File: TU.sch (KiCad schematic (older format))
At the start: 5 parts, among them J1 Conn_01x06_Male, J2 Conn_01x06_Male, J3 Conn_Coaxial, J4 Debugger, SW1 SW_DPST_x2

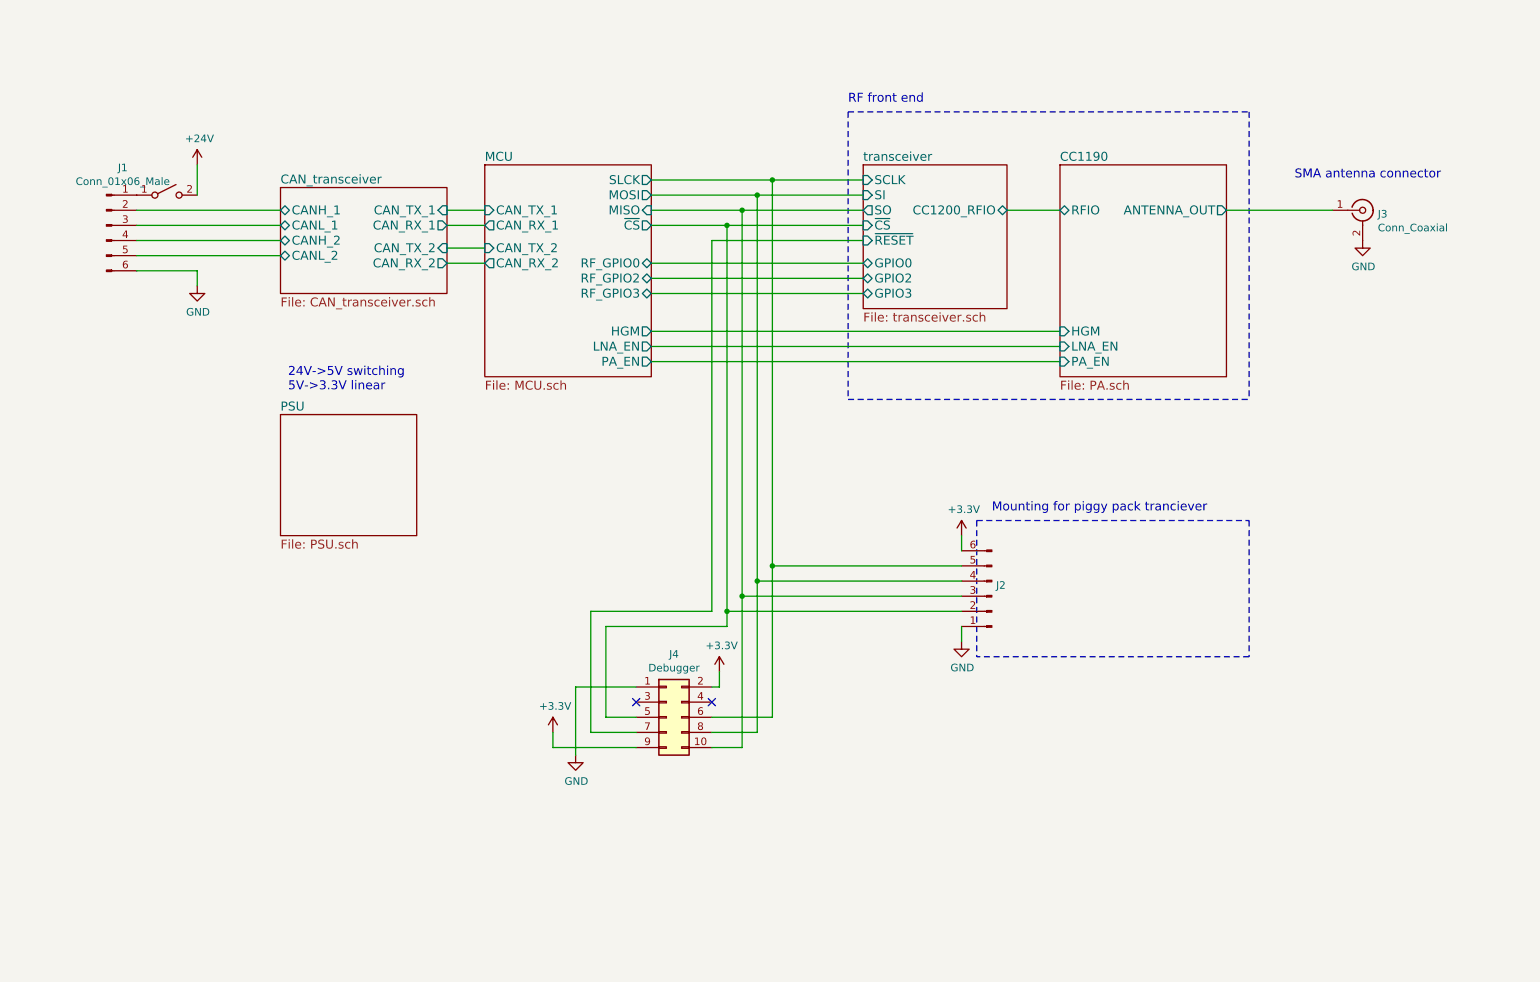
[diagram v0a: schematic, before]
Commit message: Added mount for RFM98/95
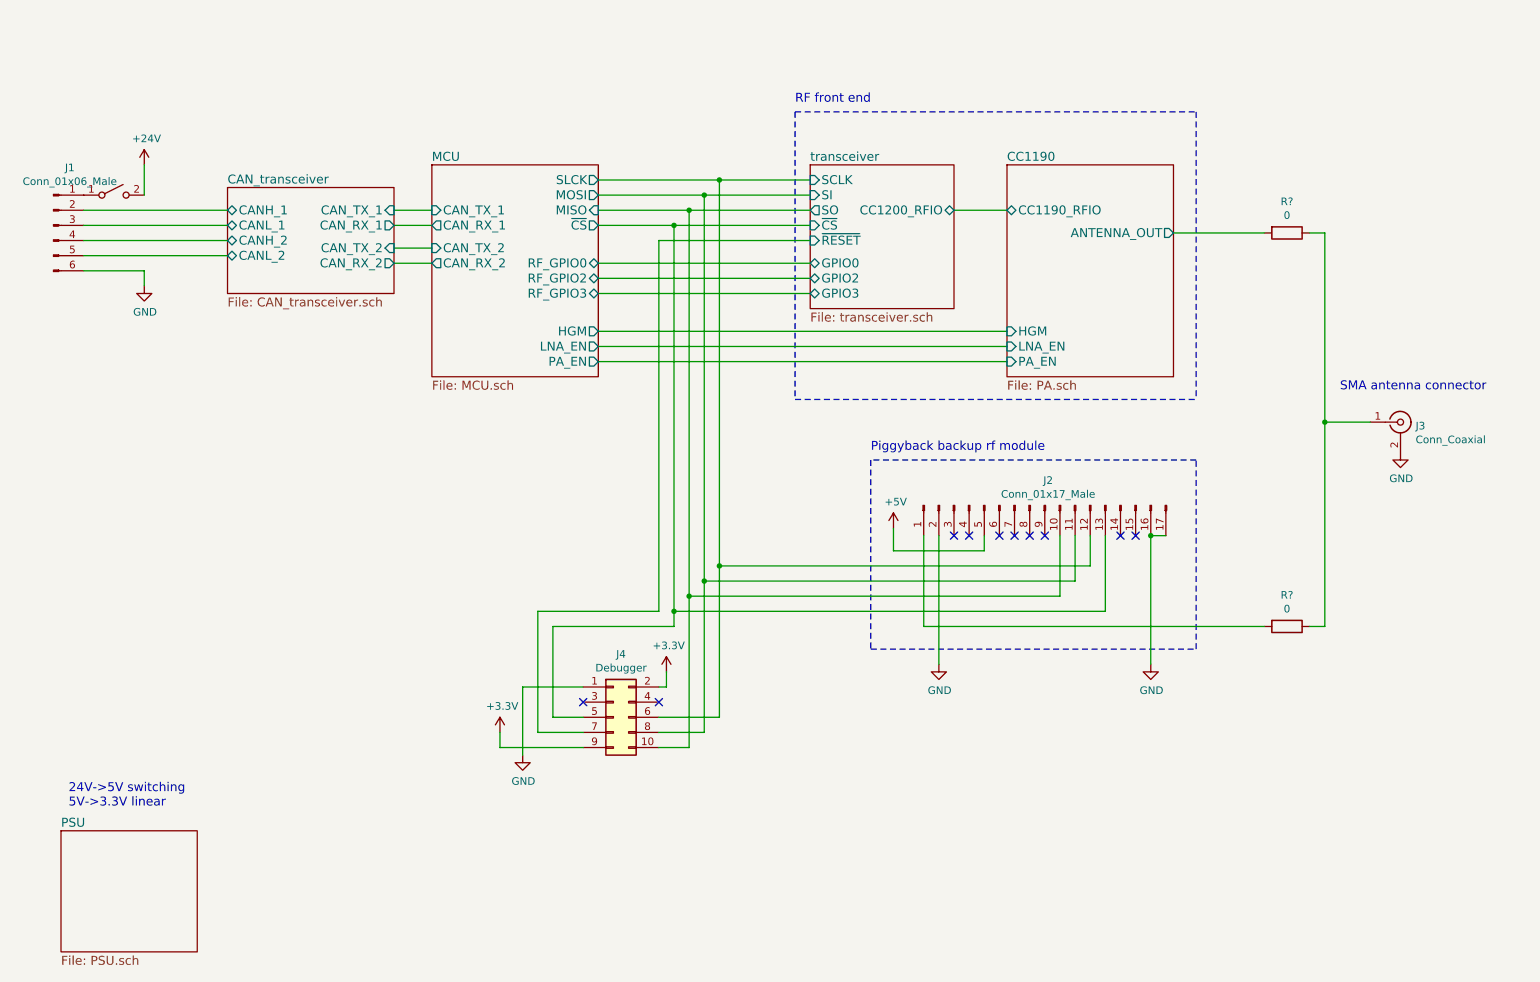
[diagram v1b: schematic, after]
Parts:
- removed J2: Conn_01x06_Male, symbol Connector:Conn_01x06_Male
- added J2: Conn_01x17_Male, symbol Connector:Conn_01x17_Male
- added R? (x2): 0, symbol Device:R
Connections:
- net CC1190/ANTENNA_OUT: now also R?.2; no longer J3.1 (In)
- net GND: now also J2.16 (Pin_16), J2.17 (Pin_17), J2.2 (Pin_2)
- net MCU/MISO: now also J2.10 (Pin_10)
- net MCU/MOSI: now also J2.11 (Pin_11)
- net MCU/SLCK: now also J2.12 (Pin_12)
- net MCU/~CS: now also J2.13 (Pin_13)
- new net: J2.1 (Pin_1), R?.2
- new net: J3.1 (In), R?.1, R?.1
- new net +5V: J2.5 (Pin_5)
- no-connect marks 2 -> 10
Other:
- note added: "Piggyback backup rf module"
- note removed: "Mounting for piggy pack tranciever"
- moved on the sheet: J1, J3, J4

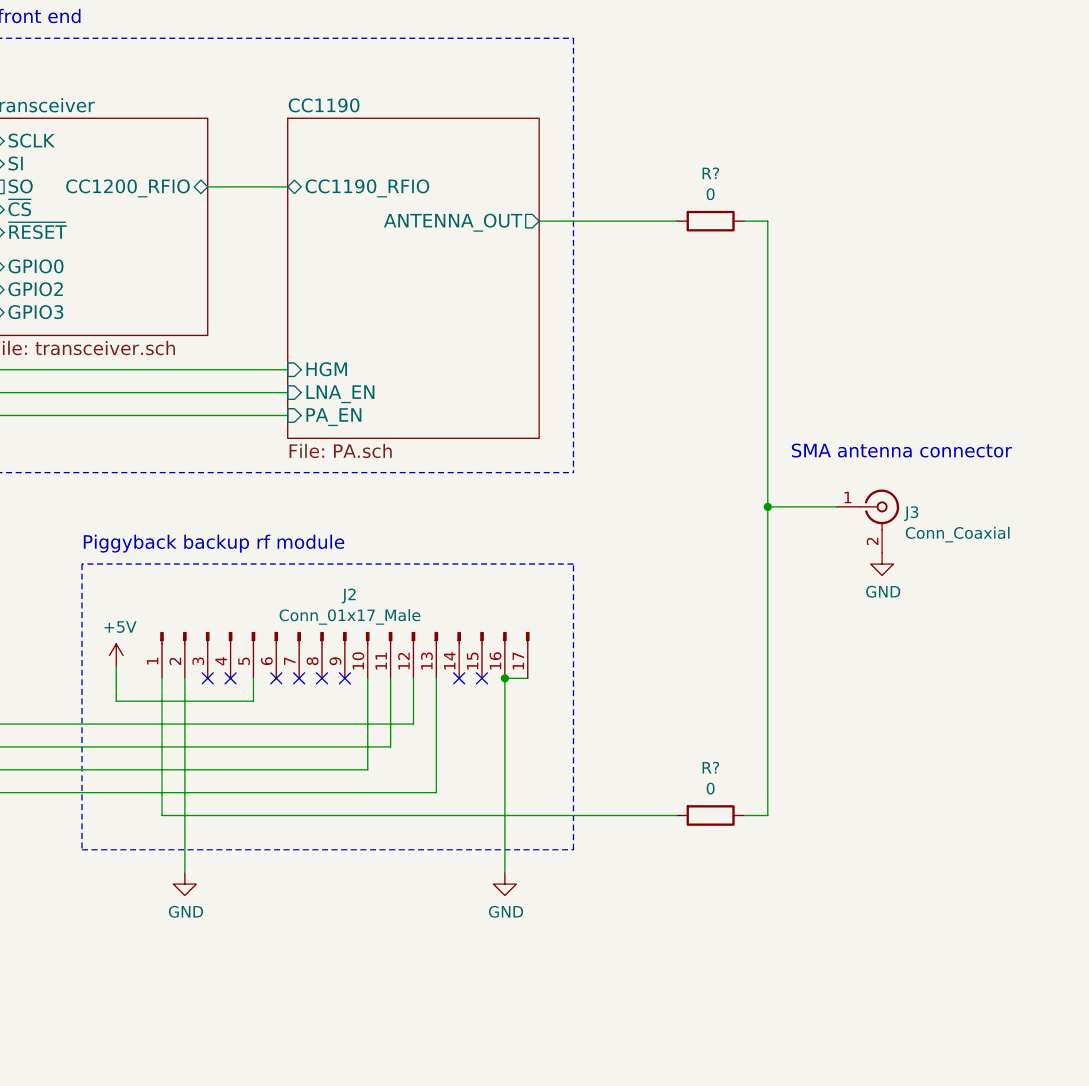
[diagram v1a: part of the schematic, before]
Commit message: Added component values for tranciever and PA
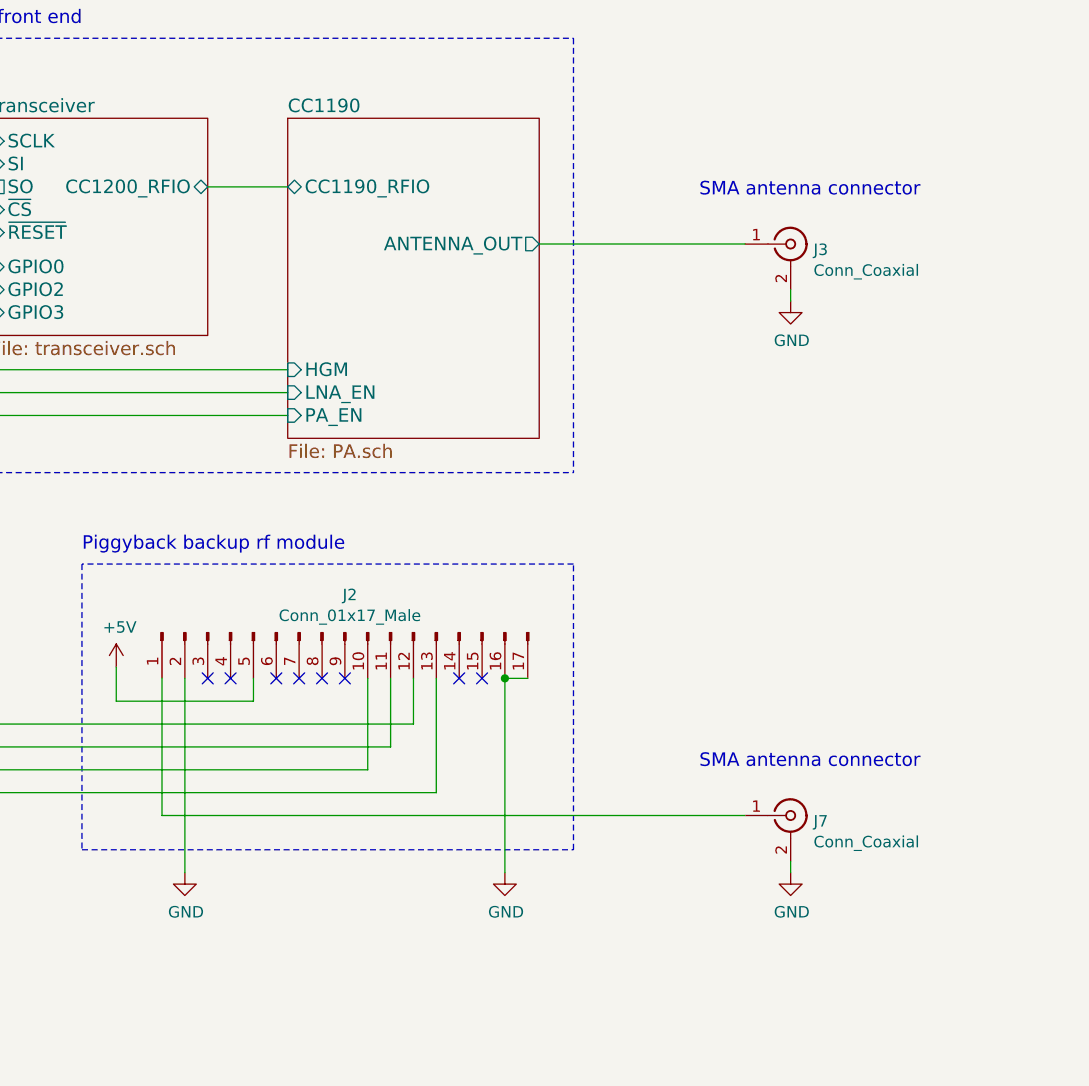
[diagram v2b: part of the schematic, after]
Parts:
- removed R? (x2): 0, symbol Device:R
- added J7: Conn_Coaxial, symbol Connector:Conn_Coaxial
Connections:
- net CC1190/ANTENNA_OUT: now also J3.1 (In)
- net GND: now also J7.2 (Ext)
- net at J2.1 (Pin_1): now also J7.1 (In)
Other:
- moved on the sheet: J3
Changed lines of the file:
@@
 F1 "PSU.sch" 59
 $EndSheet
-Wire Wire Line
-	8600 2350 9200 2350
 $Comp
 L power:+24V #PWR0103
@@
 L Connector:Conn_Coaxial J3
 U 1 1 60221CCA
-P 10100 3600
-F 0 "J3" H 10200 3575 50  0000 L CNN
-F 1 "Conn_Coaxial" H 10200 3484 50  0000 L CNN
-F 2 "" H 10100 3600 50  0001 C CNN
-F 3 " ~" H 10100 3600 50  0001 C CNN
-	1    10100 3600
+P 9700 2450
+F 0 "J3" H 9800 2425 50  0000 L CNN
+F 1 "Conn_Coaxial" H 9800 2334 50  0000 L CNN
+F 2 "" H 9700 2450 50  0001 C CNN
+F 3 " ~" H 9700 2450 50  0001 C CNN
+	1    9700 2450
 	1    0    0    -1
 $EndComp
@@
 L power:GND #PWR01
 U 1 1 60222AF8
-P 10100 3800
-F 0 "#PWR01" H 10100 3550 50  0001 C CNN
-F 1 "GND" H 10105 3627 50  0000 C CNN
-F 2 "" H 10100 3800 50  0001 C CNN
-F 3 "" H 10100 3800 50  0001 C CNN
-	1    10100 3800
-	1    0    0    -1
-$EndComp
-Text Notes 9700 3400 0    59   ~ 0
+P 9700 2700
+F 0 "#PWR01" H 9700 2450 50  0001 C CNN
+F 1 "GND" H 9705 2527 50  0000 C CNN
+F 2 "" H 9700 2700 50  0001 C CNN
+F 3 "" H 9700 2700 50  0001 C CNN
+	1    9700 2700
+	1    0    0    -1
+$EndComp
+Text Notes 9300 2250 0    59   ~ 0
 SMA antenna connector
 $Comp
@@
 F3 "LNA_EN" I L 7500 3100 59
 F4 "PA_EN" I L 7500 3200 59
-F5 "ANTENNA_OUT" O R 8600 2350 59
+F5 "ANTENNA_OUT" O R 8600 2450 59
 F6 "CC1190_RFIO" B L 7500 2200 59
 $EndSheet
@@
 Wire Wire Line
 	5200 2400 6200 2400
-$Sheet
-S 6200 1900 950  950
-U 60145F44
-F0 "transceiver" 59
-F1 "transceiver.sch" 59
-F2 "SCLK" I L 6200 2000 59
-F3 "SI" I L 6200 2100 59
-F4 "SO" O L 6200 2200 59
-F5 "~CS" I L 6200 2300 59
-F6 "~RESET" I L 6200 2400 59
-F7 "GPIO0" B L 6200 2550 59
-F8 "GPIO2" B L 6200 2650 59
-F9 "GPIO3" B L 6200 2750 59
-F10 "CC1200_RFIO" B R 7150 2200 59
-$EndSheet
 $Sheet
 S 3700 1900 1100 1400
@@
 Text Notes 6600 3800 0    59   ~ 0
 Piggyback backup rf module
-$Comp
-L Device:R R?
-U 1 1 60249BC1
-P 9350 2350
-F 0 "R?" V 9143 2350 50  0000 C CNN
-F 1 "0" V 9234 2350 50  0000 C CNN
-F 2 "" V 9280 2350 50  0001 C CNN
-F 3 "~" H 9350 2350 50  0001 C CNN
-	1    9350 2350
-	0    1    1    0
-$EndComp
-Wire Wire Line
-	9500 2350 9600 2350
-Wire Wire Line
-	9600 3600 9900 3600
 Wire Wire Line
 	8050 4550 8050 4350
@@
 	6950 4350 6950 4950
 $Comp
-L Device:R R?
-U 1 1 6025C1DB
-P 9350 4950
-F 0 "R?" V 9143 4950 50  0000 C CNN
-F 1 "0" V 9234 4950 50  0000 C CNN
-F 2 "" V 9280 4950 50  0001 C CNN
-F 3 "~" H 9350 4950 50  0001 C CNN
-	1    9350 4950
-	0    1    1    0
-$EndComp
-Wire Wire Line
-	9500 4950 9600 4950
-Wire Wire Line
-	9200 4950 6950 4950
-$Comp
-L power:GND #PWR?
+L power:GND #PWR072
 U 1 1 60260077
 P 7050 5200
-F 0 "#PWR?" H 7050 4950 50  0001 C CNN
+F 0 "#PWR072" H 7050 4950 50  0001 C CNN
 F 1 "GND" H 7055 5027 50  0000 C CNN
 F 2 "" H 7050 5200 50  0001 C CNN
@@
 Connection ~ 8450 4350
 $Comp
-L power:GND #PWR?
+L power:GND #PWR073
 U 1 1 602650C2
 P 8450 5200
-F 0 "#PWR?" H 8450 4950 50  0001 C CNN
+F 0 "#PWR073" H 8450 4950 50  0001 C CNN
 F 1 "GND" H 8455 5027 50  0000 C CNN
 F 2 "" H 8450 5200 50  0001 C CNN
@@
 	6750 4450 6750 4300
 $Comp
-L power:+5V #PWR?
+L power:+5V #PWR069
 U 1 1 60273B55
 P 6750 4300
-F 0 "#PWR?" H 6750 4150 50  0001 C CNN
+F 0 "#PWR069" H 6750 4150 50  0001 C CNN
 F 1 "+5V" H 6765 4473 50  0000 C CNN
 F 2 "" H 6750 4300 50  0001 C CNN
@@
 	1    0    0    -1
 $EndComp
-Connection ~ 9600 3600
-Wire Wire Line
-	9600 3600 9600 4950
-Wire Wire Line
-	9600 2350 9600 3600
 Wire Notes Line
 	8750 3850 6600 3850
@@
 Wire Wire Line
 	8150 4850 8150 4350
+Wire Wire Line
+	8600 2450 9500 2450
+$Comp
+L Connector:Conn_Coaxial J7
+U 1 1 601D2CAA
+P 9700 4950
+F 0 "J7" H 9800 4925 50  0000 L CNN
+F 1 "Conn_Coaxial" H 9800 4834 50  0000 L CNN
+F 2 "" H 9700 4950 50  0001 C CNN
+F 3 " ~" H 9700 4950 50  0001 C CNN
+	1    9700 4950
+	1    0    0    -1
+$EndComp
+$Comp
+L power:GND #PWR074
+U 1 1 601D2CB0
+P 9700 5200
+F 0 "#PWR074" H 9700 4950 50  0001 C CNN
+F 1 "GND" H 9705 5027 50  0000 C CNN
+F 2 "" H 9700 5200 50  0001 C CNN
+F 3 "" H 9700 5200 50  0001 C CNN
+	1    9700 5200
+	1    0    0    -1
+$EndComp
+Text Notes 9300 4750 0    59   ~ 0
+SMA antenna connector
+Wire Wire Line
+	6950 4950 9500 4950
+Wire Wire Line
+	9700 5200 9700 5150
+Wire Wire Line
+	9700 2700 9700 2650
+$Sheet
+S 6200 1900 950  950
+U 60145F44
+F0 "transceiver" 59
+F1 "transceiver.sch" 59
+F2 "SCLK" I L 6200 2000 59
+F3 "SI" I L 6200 2100 59
+F4 "SO" O L 6200 2200 59
+F5 "~CS" I L 6200 2300 59
+F6 "~RESET" I L 6200 2400 59
+F7 "GPIO0" B L 6200 2550 59
+F8 "GPIO2" B L 6200 2650 59
+F9 "GPIO3" B L 6200 2750 59
+F10 "CC1200_RFIO" B R 7150 2200 59
+$EndSheet
 $EndSCHEMATC

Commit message: Small changes to schematic
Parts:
- J4: value Debugger -> Debugger connector
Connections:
- net GND: no longer J2.17 (Pin_17)

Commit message: Changes to PA layout
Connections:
- net MCU/~CS renamed MCU/~CS_2
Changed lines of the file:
@@
 F 0 "SW1" H 1600 2335 50  0001 C CNN
 F 1 "SW_DPST_x2" H 1600 2244 50  0001 C CNN
-F 2 "" H 1600 2100 50  0000 C CNN
+F 2 "" H 1600 2100 50  0001 C CNN
 F 3 "~" H 1600 2100 50  0001 C CNN
 	1    1600 2100
@@
 Connection ~ 5400 2200
 Wire Wire Line
-	5300 2300 6200 2300
-Connection ~ 5300 2300
-Wire Wire Line
 	5200 2400 6200 2400
-$Sheet
-S 3700 1900 1100 1400
-U 60144E24
-F0 "MCU" 59
-F1 "MCU.sch" 59
-F2 "SLCK" O R 4800 2000 59
-F3 "MOSI" O R 4800 2100 59
-F4 "MISO" I R 4800 2200 59
-F5 "~CS" O R 4800 2300 59
-F6 "CAN_TX_1" I L 3700 2200 59
-F7 "CAN_RX_1" O L 3700 2300 59
-F8 "CAN_TX_2" I L 3700 2450 59
-F9 "CAN_RX_2" O L 3700 2550 59
-F10 "HGM" O R 4800 3000 59
-F11 "LNA_EN" O R 4800 3100 59
-F12 "PA_EN" O R 4800 3200 59
-F13 "RF_GPIO0" B R 4800 2550 59
-F14 "RF_GPIO2" B R 4800 2650 59
-F15 "RF_GPIO3" B R 4800 2750 59
-$EndSheet
 Wire Wire Line
 	3450 2200 3700 2200
@@
 Wire Wire Line
 	4800 2200 5400 2200
-Wire Wire Line
-	4800 2300 5300 2300
 Wire Wire Line
 	4800 2550 6200 2550
@@
 Wire Wire Line
 	5300 4950 5300 4850
-Wire Wire Line
-	5300 2300 5300 4850
-Connection ~ 5300 4850
 Wire Notes Line
 	6600 3850 6600 5100
@@
 F9 "CANL_2" B L 2350 2500 59
 $EndSheet
+$Sheet
+S 3700 1900 1100 1400
+U 60144E24
+F0 "MCU" 59
+F1 "MCU.sch" 59
+F2 "SLCK" O R 4800 2000 59
+F3 "MOSI" O R 4800 2100 59
+F4 "MISO" I R 4800 2200 59
+F5 "CAN_TX_1" I L 3700 2200 59
+F6 "CAN_RX_1" O L 3700 2300 59
+F7 "CAN_TX_2" I L 3700 2450 59
+F8 "CAN_RX_2" O L 3700 2550 59
+F9 "HGM" O R 4800 3000 59
+F10 "LNA_EN" O R 4800 3100 59
+F11 "PA_EN" O R 4800 3200 59
+F12 "RF_GPIO0" B R 4800 2550 59
+F13 "RF_GPIO2" B R 4800 2650 59
+F14 "RF_GPIO3" B R 4800 2750 59
+F15 "~CS_2" O R 4800 2450 59
+F16 "~CS_1" O R 4800 2300 59
+$EndSheet
+Wire Wire Line
+	4800 2300 6200 2300
+Wire Wire Line
+	5300 4850 5300 2450
+Wire Wire Line
+	5300 2450 4800 2450
+Connection ~ 5300 4850
 $EndSCHEMATC

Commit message: Lots of work on routing and pcb layout
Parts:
- removed SW1: SW_DPST_x2, symbol Switch:SW_DPST_x2
- J1: footprint (none) -> Connector_PinHeader_2.54mm:PinHeader_1x06_P2.54mm_Vertical
- J2: footprint (none) -> KTHFS:RFM95PW
- J3, J7: footprint (none) -> Connector_Coaxial:SMA_Amphenol_132134-10_Vertical
- J4: footprint (none) -> Connector_PinHeader_2.54mm:PinHeader_2x05_P2.54mm_Vertical
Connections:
- net battery_in: now reaches J1.1 (Pin_1)
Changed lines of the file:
@@
 F0 "PSU" 59
 F1 "PSU.sch" 59
+F2 "battery_in" I L 1800 5475 59
 $EndSheet
-$Comp
-L power:+24V #PWR0103
-U 1 1 6015CE4B
-P 1800 1900
-F 0 "#PWR0103" H 1800 1750 50  0001 C CNN
-F 1 "+24V" H 1815 2073 50  0000 C CNN
-F 2 "" H 1800 1900 50  0001 C CNN
-F 3 "" H 1800 1900 50  0001 C CNN
-	1    1800 1900
-	1    0    0    -1
-$EndComp
 Wire Wire Line
 	1800 2600 1800 2700
@@
 F 0 "J3" H 9800 2425 50  0000 L CNN
 F 1 "Conn_Coaxial" H 9800 2334 50  0000 L CNN
-F 2 "" H 9700 2450 50  0001 C CNN
+F 2 "Connector_Coaxial:SMA_Amphenol_132134-10_Vertical" H 9700 2450 50  0001 C CNN
 F 3 " ~" H 9700 2450 50  0001 C CNN
 	1    9700 2450
@@
 F 0 "J1" H 1308 2681 50  0000 C CNN
 F 1 "Conn_01x06_Male" H 1308 2590 50  0000 C CNN
-F 2 "" H 1200 2300 50  0001 C CNN
+F 2 "Connector_PinHeader_2.54mm:PinHeader_1x06_P2.54mm_Vertical" H 1200 2300 50  0001 C CNN
 F 3 "~" H 1200 2300 50  0001 C CNN
 	1    1200 2300
-	1    0    0    -1
-$EndComp
-Wire Wire Line
-	1800 1900 1800 2100
-$Comp
-L Switch:SW_DPST_x2 SW1
-U 1 1 6018598A
-P 1600 2100
-F 0 "SW1" H 1600 2335 50  0001 C CNN
-F 1 "SW_DPST_x2" H 1600 2244 50  0001 C CNN
-F 2 "" H 1600 2100 50  0001 C CNN
-F 3 "~" H 1600 2100 50  0001 C CNN
-	1    1600 2100
 	1    0    0    -1
 $EndComp
@@
 F 0 "J7" H 9800 4925 50  0000 L CNN
 F 1 "Conn_Coaxial" H 9800 4834 50  0000 L CNN
-F 2 "" H 9700 4950 50  0001 C CNN
+F 2 "Connector_Coaxial:SMA_Amphenol_132134-10_Vertical" H 9700 4950 50  0001 C CNN
 F 3 " ~" H 9700 4950 50  0001 C CNN
 	1    9700 4950
@@
 F 0 "J4" H 4875 5950 50  0000 C CNN
 F 1 "Debugger connector" H 4875 5875 50  0000 C CNN
-F 2 "" H 4900 5550 50  0001 C CNN
+F 2 "Connector_PinHeader_2.54mm:PinHeader_2x05_P2.54mm_Vertical" H 4900 5550 50  0001 C CNN
 F 3 "~" H 4900 5550 50  0001 C CNN
 	1    4900 5550
@@
 F 0 "J2" V 7585 4128 50  0000 C CNN
 F 1 "Conn_01x17_Male" V 7676 4128 50  0000 C CNN
-F 2 "" H 7750 4150 50  0001 C CNN
+F 2 "KTHFS:RFM95PW" H 7750 4150 50  0001 C CNN
 F 3 "~" H 7750 4150 50  0001 C CNN
 	1    7750 4150
@@
 	5300 2450 4800 2450
 Connection ~ 5300 4850
+Text Label 2100 2100 2    59   ~ 0
+battery_in
+Wire Wire Line
+	1400 2100 2100 2100
+Text Label 1100 5475 0    59   ~ 0
+battery_in
+Wire Wire Line
+	1800 5475 1100 5475
 $EndSCHEMATC
